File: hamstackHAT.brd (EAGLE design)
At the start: 65 x 56 mm, 14 parts, among them K2 RASPI_HEADER, U1 TXB0108PWR

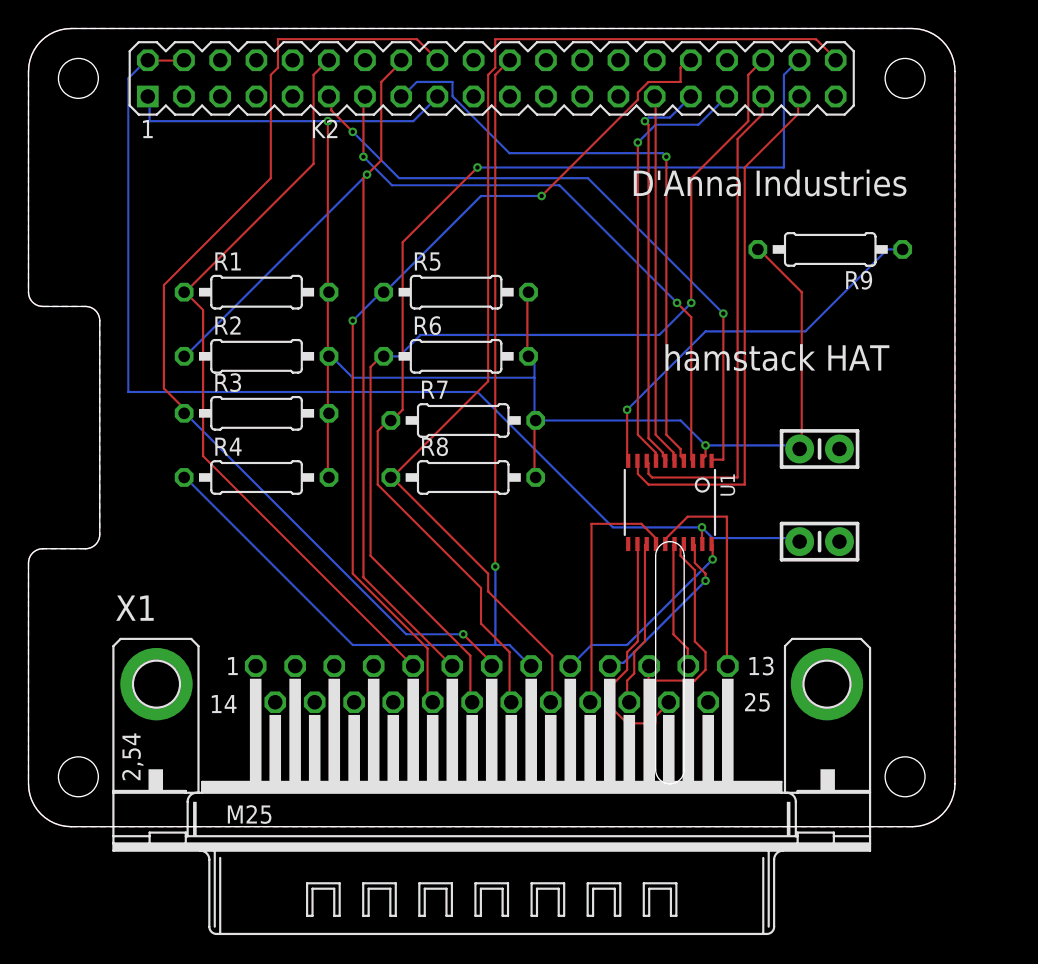
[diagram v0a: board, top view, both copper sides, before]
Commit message: re-arange everythign to imporove routing
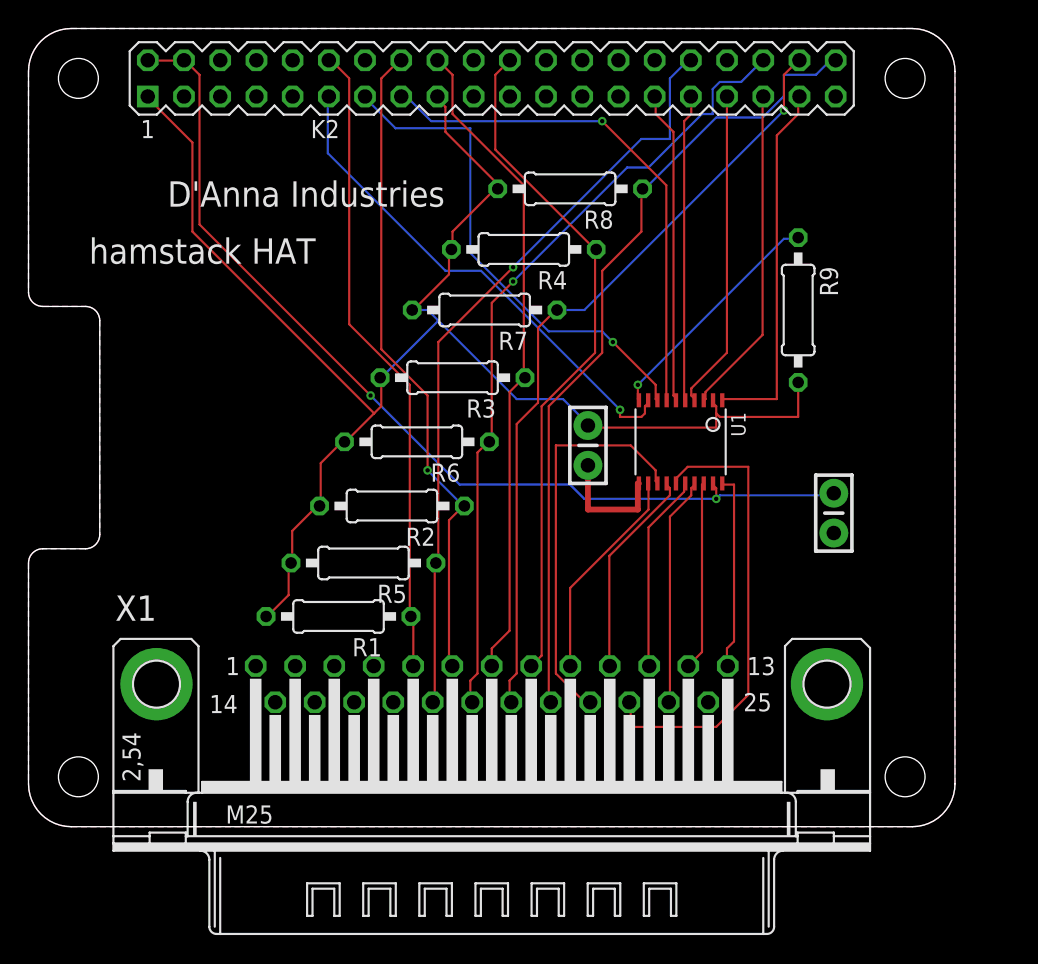
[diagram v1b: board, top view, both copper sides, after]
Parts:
- moved R4 24.6 mm to (34.8, 40.5), turned to 180 degrees
- moved R1 23.5 mm to (21.8, 14.8), turned to 180 degrees
- moved R8 21.6 mm to (38.0, 44.8), turned to 180 degrees
- moved R5 20.1 mm to (23.5, 18.5), turned to 180 degrees
- moved C3 16.3 mm to (39.2, 26.8), turned to 270 degrees
- moved R2 14.2 mm to (25.5, 22.5), turned to 180 degrees
- moved R3 14.0 mm to (29.8, 31.5), turned to 180 degrees
- moved R7 7.89 mm to (32.0, 36.2), turned to 180 degrees
- moved R6 6.60 mm to (27.2, 27.0), turned to 180 degrees
- moved R9 4.81 mm to (54.0, 36.2), turned to 270 degrees
- moved U1 4.32 mm to (45.8, 27.0)
- moved C1 2.24 mm to (56.5, 22.0), turned to 270 degrees
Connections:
- net DIGIN10: now also U1.14; no longer U1.18
- net DIGIN11: now also U1.16; no longer U1.17
- net DIGIN12: now also U1.18; no longer U1.16
- net DIGIN13: now also U1.20; no longer U1.15
- net DIGIN22: now also U1.13; no longer U1.14
- net DIGIN23: now also U1.15; no longer U1.13
- net DIGIN24: now also U1.17; no longer U1.12
- net DIGIN9: now also U1.12; no longer U1.20
- net GPIO13: now also U1.4; no longer U1.7
- net GPIO17: now also U1.9; no longer U1.1
- net GPIO19: now also U1.3; no longer U1.8
- net GPIO22: now also U1.7; no longer U1.4
- net GPIO26: now also U1.1; no longer U1.9
- net GPIO27: now also U1.8; no longer U1.3
- net GPIO5: now also U1.6; no longer U1.5
- net GPIO6: now also U1.5; no longer U1.6
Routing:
- net DIGO7: track 71.1 -> 46.0 mm, vias 1 -> 0
- net DIGO8: track 71.4 -> 47.8 mm, vias 1 -> 0
- net DIGO21: track 78.9 -> 57.1 mm
- net DIGIN23: track 11.8 -> 32.7 mm
- net DIGO20: track 74.0 -> 54.8 mm
- net DIGO6: track 64.4 -> 46.2 mm
- net DIGO19: track 70.0 -> 56.0 mm
- net GPIO26: track 37.5 -> 25.7 mm
- net GPIO19: track 34.8 -> 23.0 mm
- net N$20: track 27.6 -> 16.7 mm
- net +5V: track 79.1 -> 68.5 mm, vias 1 -> 2
- net GPIO17: track 45.6 -> 35.3 mm, vias 2 -> 1
- net DIGIN22: track 17.9 -> 28.1 mm
- net GND: track 0.00 -> 8.51 mm
- net DIGO5: track 53.4 -> 45.2 mm
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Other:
- outline, holes or cut-outs redrawn
